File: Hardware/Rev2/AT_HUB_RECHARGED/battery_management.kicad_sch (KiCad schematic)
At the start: 35 parts, among them J13 Pack Thermister, J14 Through Hole, J15 EXT Charge Port, J16 USB_C_Receptacle_PowerOnly_6P, J2 JST, SW11 SW_SPDT, U7 BQ21040DBV, U8 TLV61070ADBV, U9 BQ27427YZFR

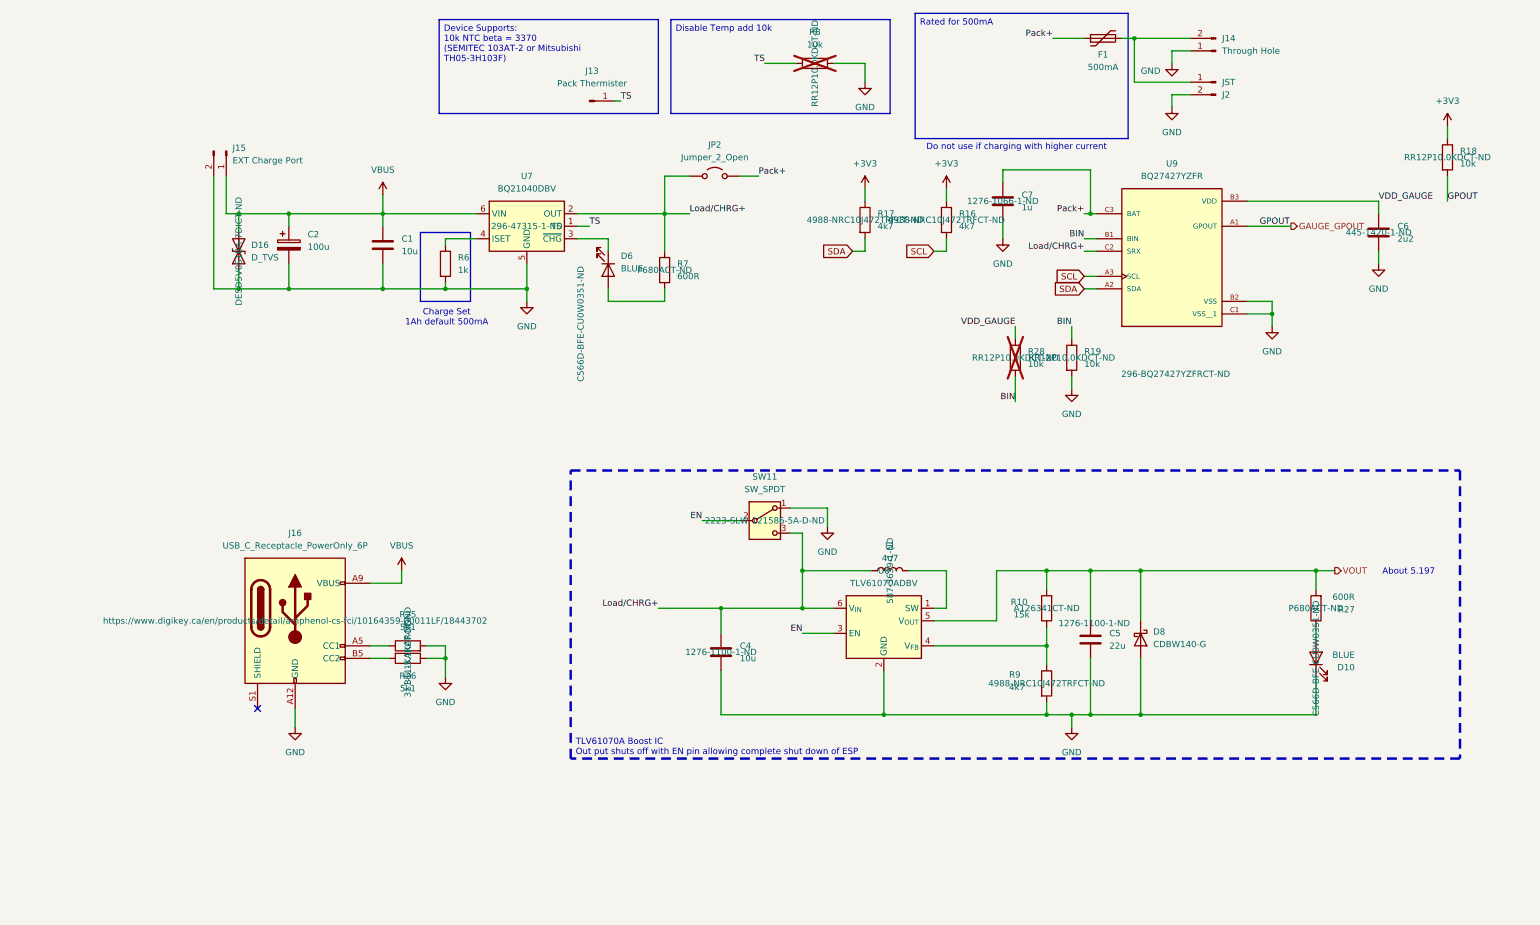
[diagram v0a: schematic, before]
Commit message: Added new protections and load sharing for lipo, also changed inductor to be autoplaced
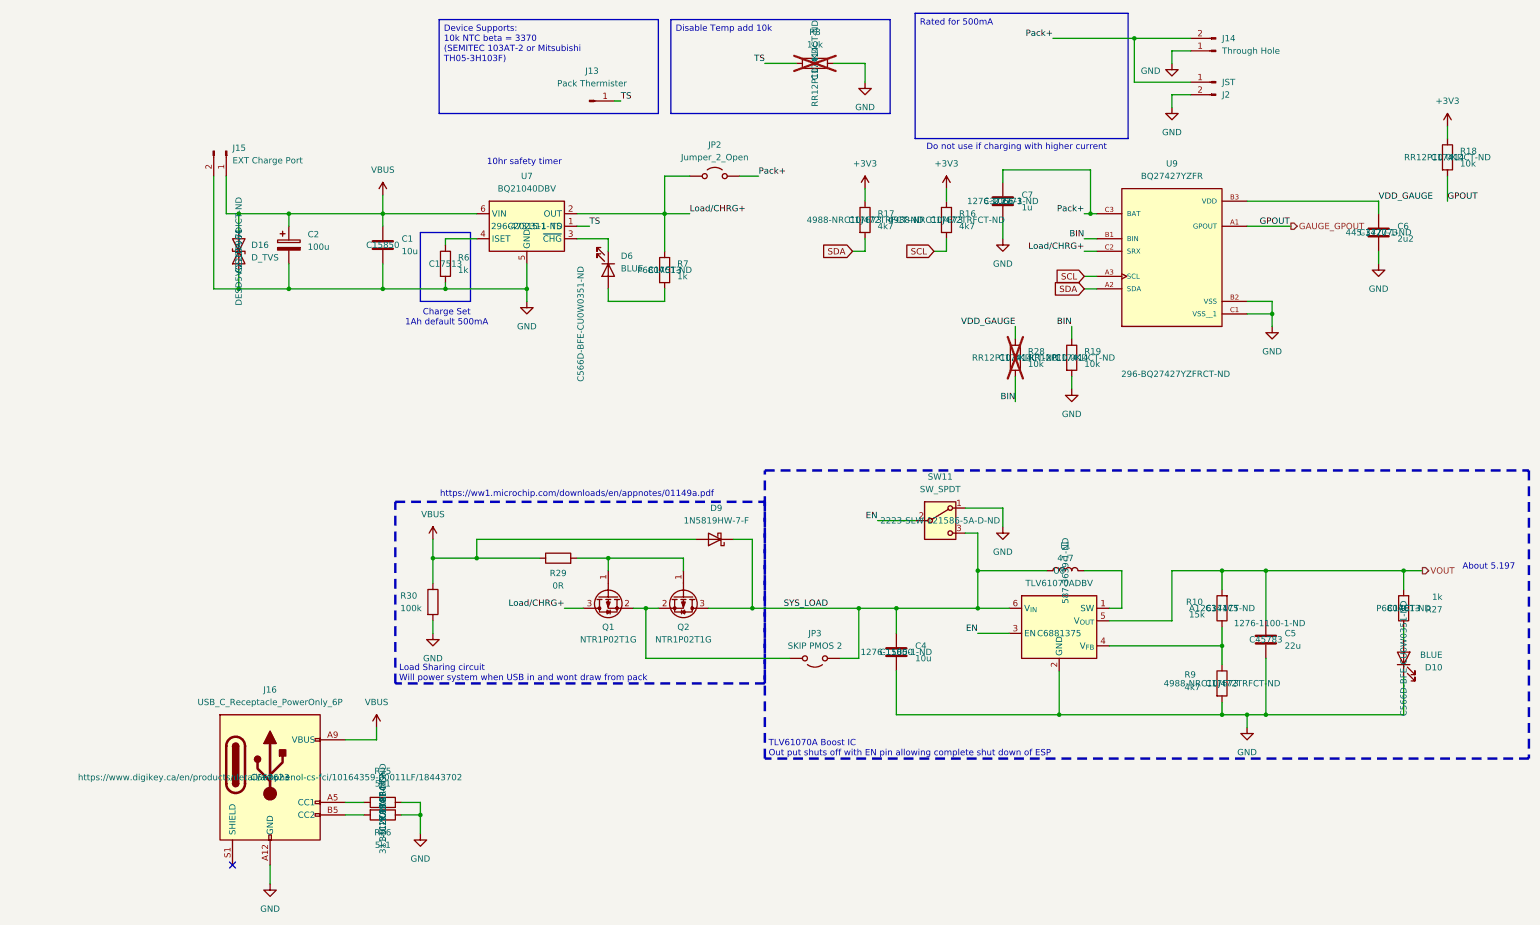
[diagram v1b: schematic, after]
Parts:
- removed D8: CDBW140-G, Diode_SMD:D_SOD-123, symbol Device:D_Schottky
- removed F1: 500mA, Fuse:Fuse_1206_3216Metric, symbol Device:Polyfuse
- added D9: 1N5819HW-7-F, Diode_SMD:D_SOD-123, symbol Device:D_Schottky
- added JP3: SKIP PMOS 2, Jumper:SolderJumper-2_P1.3mm_Open_RoundedPad1.0x1.5mm, symbol Jumper:Jumper_2_Open
- added Q1, Q2: NTR1P02T1G, Package_TO_SOT_SMD:SOT-23, symbol Transistor_FET:Q_PMOS_GSD
- added R29: 0R, Resistor_SMD:R_0805_2012Metric, symbol Device:R
- added R30: 100k, Resistor_SMD:R_0805_2012Metric, symbol Device:R
- C1, C4: LCSC (none) -> C15850
- C5: LCSC (none) -> C45783
- C6: LCSC (none) -> C377773
- C7: Adjusted Value for stock (none) -> 2.2u; LCSC (none) -> C377773
- D16: LCSC (none) -> C2157964
- J16: LCSC (none) -> C668623
- L1: footprint Inductor_SMD:L_Taiyo-Yuden_NR-60xx -> AT_HUB_R2:Ceaiya SMD,6x6mm CR6028-2R2N
- R10: LCSC (none) -> C17475
- R16, R17, R9: LCSC (none) -> C17673
- R18, R19, R28, R8: LCSC (none) -> C17414
- R25, R26: LCSC (none) -> C27834
- R27, R7: value 600R -> 1k; LCSC (none) -> C17513
- R6: LCSC (none) -> C17513
- U7: LCSC (none) -> C202311
- U8: LCSC (none) -> C6881375
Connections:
- net GND: now also R30.2
- net Load/CHRG+: now also Q1.3 (D); no longer C4.1, L1.1, SW11.3 (C), U8.6 (V_{IN})
- net Pack+: now also J14.2 (Pin_2), J2.1 (Pin_1)
- net VBUS: now also D9.2 (A), R29.1, R30.1
- new net: JP3.2 (B), Q1.2 (S), Q2.2 (S)
- new net: Q1.1 (G), Q2.1 (G), R29.2
- new net SYS_LOAD: C4.1, D9.1 (K), JP3.1 (A), L1.1, Q2.3 (D), SW11.3 (C), U8.6 (V_{IN})
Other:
- note added: "10hr safety timer"
- note added: "Load Sharing circuit Will power system when USB in and wont draw from pack"
- note added: "https://ww1.microchip.com/downloads/en/appnotes/01149a.pdf"
- moved on the sheet: C4, C5, D10, J16, L1, R10, R25, R26, R27, R9, SW11, U8

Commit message: A
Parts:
- L1: LCSC (none) -> C520367
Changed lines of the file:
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@@
 			)
 		)
-		(property "LCSC" ""
+		(property "LCSC" "C520367"
 			(at 189.23 125.73 0)
 			(effects

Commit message: Changed net label for charging subcircuit to Bat+
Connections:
- net Load/CHRG+ renamed Bat+
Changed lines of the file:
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@@
 			"L1dJTkRPV1MvZm9udHNcTU9EMjAuVFRGAAAAAAAAAAAAAAAAAADBK53XAI4DgMCR14cqAgAAAwAA"
 			"AAAAAAAAssaHKgIAAAEAAAAAAAAAAAAAAAAAAADEK5jXAI8DgAAAAAAAAAAAAwAAAAAAAADgWIyH"
-			"KgIAAAEAAAAAAAAAAAAAAAAAAAC7K5vXAJADgDCO14cqAgAAAwAAAAAAAAAwXw=="
+			"KgIAAAEAAAAAAAAAAAAAAAAAAAC7K5vXAJADgDCO14cqAgAAAwAAAAAAAAAwXwAAAAAAAHC6hqUA"
+			"gweAAAAAAAAAAAAAAAAAAAAAAAAAAAAAAAAAcrqApQCEB4AAAAAAAAAAAAAAAAAAAAAAAAAAAAAA"
+			"AABMuoKlAIUHgAAAAAAAAAAAAAAAAAAAAAAAAAAAAAAAAE66vKUAhgeAAAAAAAAAAAAAAAAAAAAA"
+			"AAAAAAAAAAAASLq+pQCHB4AAAAAAAAAAAAAAAAAAAAAAAAAAAAAAAABKurilAIgHgAAAAAAAAAAA"
+			"AAAAAAAAAAAAAAAAAAAAAES6uqUAiQeAAAAAAAAAAAAAAAAAAAAAAAAAAAAAAAAARrq0pQCKB4AA"
+			"AAAAAAAAAAAAAAAAAAAAAAAAAAAAAABAuralAIsHgAAAAAAAAAAAAAAAAAAAAAAAAAAAAAAAAEK6"
+			"sKUAjAeAAAAAAAAAAAAAAAAAAAAAAAAAAAAAAAAAXLqypQCNB4AAAAAAAAAAAAAAAAAAAAAAAAAA"
+			"AAAAAABeuqylAI4HgAAAAAAAAAAAAAAAAAAAAAAAAAAAAAAAAFi6rqUAjweAAAAAAAAAAAAAAAAA"
+			"AAAAAAAAAAAAAAAAWrqopQCQB4AAAAAAAAAAAAAAAAAAAAAAAAAAAAAAAABUuqqlAJEHgAAAAAAA"
+			"AAAAAAAAAAAAAAAAAAAAAAAAAFa6pKUAkgeAAAAAAAAAAAAAAAAAAAAAAAAAAAAAAAAAULqmpQCT"
+			"B4AAAAAAAAAAAAAAAAAAAAAAAAAAAAAAAABSuqClAJQHgAAAAAAAAAAAAAAAAAAAAAAAAAAAAAAA"
+			"ACy6oqUAlQeAAAAAAAAAAAAAAAAAAAAAAAAAAAAAAAAALrrcpQCWB4AAAAAAAAAAAAAAAAAAAAAA"
+			"AAAAAAAAAAAout6lAJcHgAAAAAAAAAAAAAAAAAAAAAAAAAAAAAAAACq62KUAmAeAAAAAAAAAAAAA"
+			"AAAAAAAAAAAAAAAAAAAAJLrapQCZB4AAAAAAAAAAAAAAAAAAAAAAAAAAAAAAAAAmutSlAJoHgAAA"
+			"AAAAAAAAAAAAAAAAAAAAAAAAAAAAACC61qUAmweAAAAAAAAAAAAAAAAAAAAAAAAAAAAAAAAAIrrQ"
+			"pQCcB4AAAAAAAAAAAAAAAAAAAAAAAAAAAAAAAAA8utKlAJ0HgAAAAAAAAAAAAAAAAAAAAAAAAAAA"
+			"AAAAAD66zKUAngeAAAAAAAAAAAAAAAAAAAAAAAAAAAAAAAAAOLrOpQCfB4AAAAAAAAAAAAAAAAAA"
+			"AAAAAAAAAAAAAAA6usilAKAHgAAAAAAAAAAAAAAAAAAAAAAAAAAAAAAAADS6yqUAoQeAAAAAAAAA"
+			"AAAAAAAAAAAAAAAAAAAAAAAANrrEpQCiB4AAAAAAAAAAAAAAAAAAAAAAAAAAAA=="
 		)
 	)
@@
 		)
 	)
-	(label "Load{slash}CHRG+"
+	(label "Bat+"
 		(at 87.63 133.35 180)
 		(effects
@@
 		)
 	)
+	(label "Bat+"
+		(at 193.04 60.96 180)
+		(effects
+			(font
+				(size 1.27 1.27)
+			)
+			(justify right bottom)
+		)
+	)
 	(label "EN"
 		(at 151.13 115.57 180)
@@
 		)
 	)
-	(label "Load{slash}CHRG+"
-		(at 113.03 53.34 0)
-		(effects
-			(font
-				(size 1.27 1.27)
-			)
-			(justify left bottom)
-		)
-	)
 	(label "BIN"
 		(at 179.07 91.44 180)
-		(effects
-			(font
-				(size 1.27 1.27)
-			)
-			(justify right bottom)
-		)
-	)
-	(label "Load{slash}CHRG+"
-		(at 193.04 60.96 180)
 		(effects
 			(font
@@
 		)
 	)
+	(label "Bat+"
+		(at 113.03 53.34 0)
+		(effects
+			(font
+				(size 1.27 1.27)
+			)
+			(justify left bottom)
+		)
+	)

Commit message: Done the design will verify
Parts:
- removed C6: 2u2, Capacitor_SMD:C_0805_2012Metric, symbol Device:C
- removed C7: 1u, Capacitor_SMD:C_0805_2012Metric, symbol Device:C
- removed U9: BQ27427YZFR, AT_HUB_R2:IC_BQ27427YZFR, symbol AT_HUB_R2:BQ27427YZFR
- added C8: 1u, Capacitor_SMD:C_0805_2012Metric, symbol Device:C
- added C9: 2u2, Capacitor_SMD:C_0805_2012Metric, symbol Device:C
- added R36: R01, Resistor_SMD:R_0805_2012Metric, symbol Device:R
- added U10: BQ27441DRZR-G1A, Package_SON:Texas_S-PDSO-N12, symbol Battery_Management:BQ27441DRZR-G1A
- L1: value 4u7 -> 2u2
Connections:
- net BIN: now also U10.10 (BIN)
- net Bat+: now also R36.1, U10.6 (BAT), U10.7 (SRN)
- net GAUGE_GPOUT: now also U10.12 (GPOUT)
- net GND: now also C8.2, C9.2, U10.13 (PAD), U10.3 (V_{SS})
- net Pack+: now also C8.1, R36.2, U10.8 (SRP)
- net SCL: now also U10.2 (SCL)
- net SDA: now also U10.1 (SDA)
- new net: C9.1, U10.5 (V_{DD})
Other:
- moved on the sheet: R18, R19, R28

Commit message: Added Rev 3
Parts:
- removed R28: 10k, Resistor_SMD:R_0805_2012Metric, symbol Device:R
- C2: footprint Capacitor_SMD:C_Elec_6.3x7.7 -> Capacitor_Tantalum_SMD:CP_EIA-3216-18_Kemet-A
- R8: now fitted
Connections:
- net Bat+: now also C8.1
- net Pack+: no longer C8.1
- net VDD_GAUGE: now also C9.1, U10.5 (V_{DD})
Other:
- moved on the sheet: C8, R16, R17, R18, R19
